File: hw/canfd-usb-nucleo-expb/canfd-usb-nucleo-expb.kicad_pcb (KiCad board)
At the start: 2 copper layers, 70 x 59 mm, 58 parts, among them CN1 Conn_02x19_Odd_Even, CN2 CONN, J1 USB_C_Receptacle_USB2.0, J2 Conn_01x10, J3 Conn_01x10, J4 Conn_01x10, SW1 SW_Push_Dual_x2, SW2 SW_Push_Dual_x2, SW3 SW_Push_Dual_x2, U1 USBLC6-2SC6, U2 ATA6561-GAQW-N, U3 ATA6561-GAQW-N, U4 ATA6561-GAQW-N

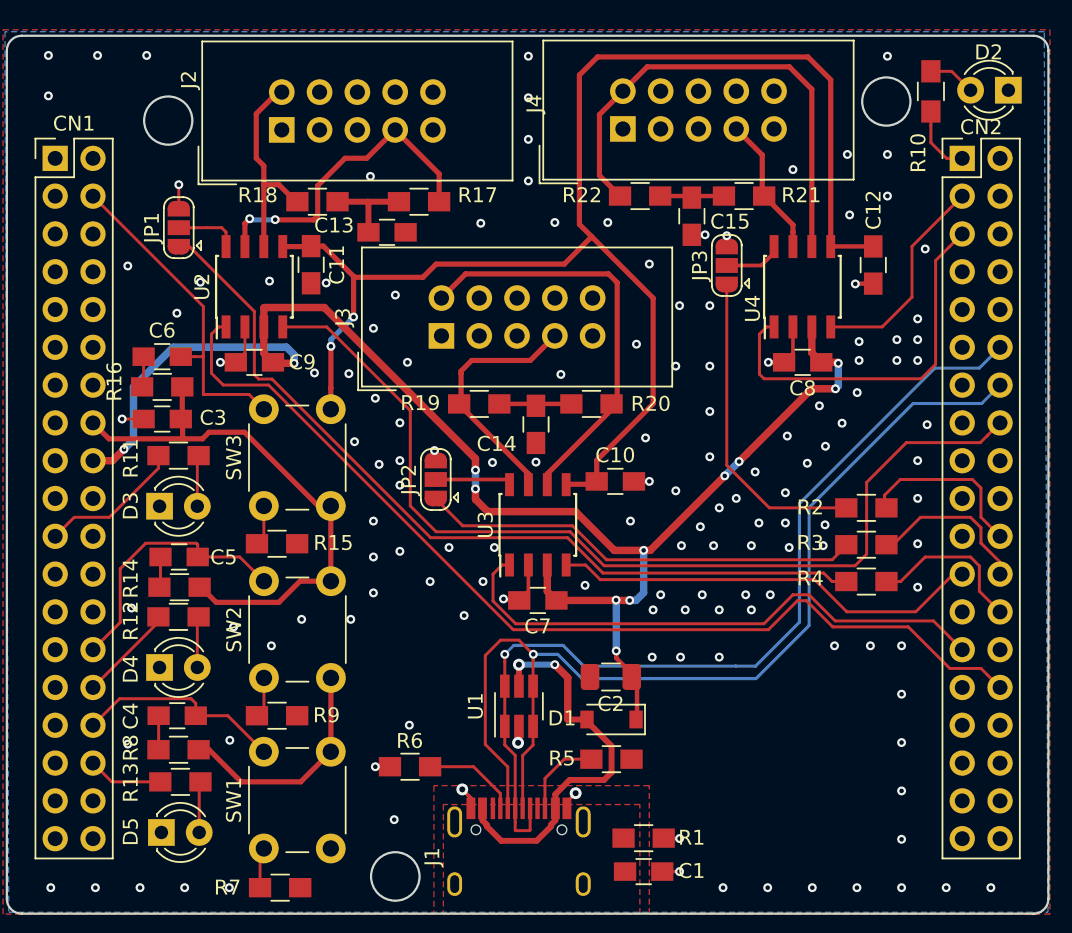
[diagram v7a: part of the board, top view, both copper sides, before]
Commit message: HW: PCB layout fix_1
Power supply lines are re-routed
More vias to Power supply lines are added
USB ESD protection symbol on the schematic is changed
ESD protection bridges beetwen data lines are removed
LED positions are remaining unchanged

Co-authored-by: Viacheslav Olizarenko <stiwenss@gmail.com>
Co-authored-by: AlexeyZ <silkt207@gmail.com>
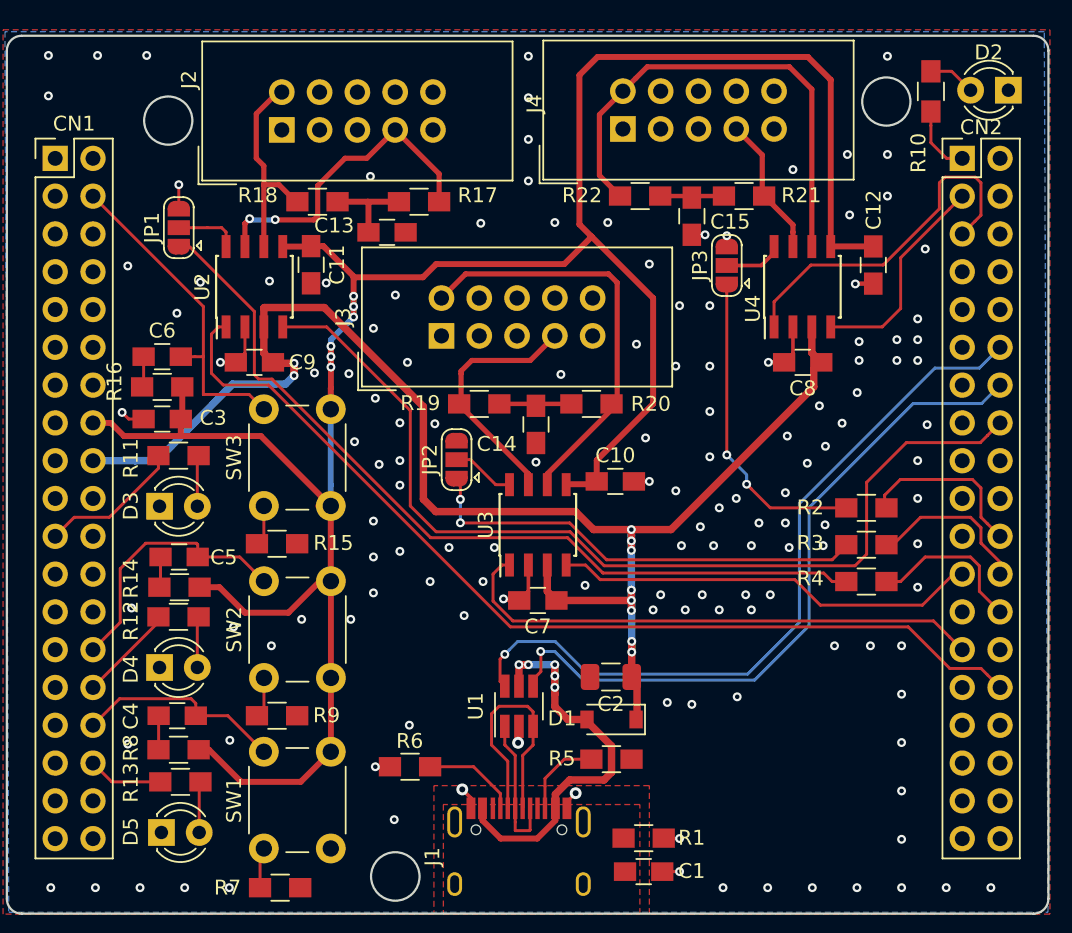
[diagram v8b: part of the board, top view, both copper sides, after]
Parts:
- moved JP2 1.93 mm to (132.5, 98.4)
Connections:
- J1 pad A6: D+ -> /D+in
- J1 pad A7: D- -> /D-in
- J1 pad B6: D+ -> /D+in
- J1 pad B7: D- -> /D-in
- U1 pad 1: D+ -> /D+in
- U1 pad 3: D- -> /D-in
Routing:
- net D-: track 70.5 -> 47.1 mm
- net +3V3: track 150.1 -> 166.8 mm, vias 2 -> 6
- net /D-in: track 0.00 -> 16.7 mm
- net D+: track 62.3 -> 50.7 mm
- net /D+in: track 0.00 -> 9.77 mm
- net /Vbus: track 26.5 -> 29.0 mm, vias 2 -> 5
- net TX2: track 37.7 -> 36.1 mm
- net TX1: track 67.2 -> 65.6 mm
- net TX3: track 25.7 -> 24.2 mm
- net STANDBY_2: track 29.4 -> 30.1 mm, vias 0 -> 2
- net Net-(JP2-Pad2): track 5.23 -> 4.65 mm
- net +5V: track 102.0 -> 102.5 mm, vias 12 -> 10
- net GND: track 26.0 -> 25.5 mm, vias 139 -> 136
- net STANDBY_3: vias 0 -> 2
